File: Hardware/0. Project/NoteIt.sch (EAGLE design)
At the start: 61 parts, among them CN1 MICROSD-PUSH-OUT, CN3 USB 3.2 Gen 2 Type C Receptac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, CN4 FTSH-105-01-L-DV-K-TR, IC2 MCP73831/OT, IC5 S-8261ACMMD-G4MT2U, Q2 SI2374DSTRPBF, Q3 SI2374DSTRPBF, Q4 BC817-16LT1SMD, SW1 KY-040, U1 SN74AHC1G125, U10 MSP430FR2476TPTR, U2 GL823K, U4 TS3A27518EPWR, U5 TLV75530PDBVR, U8 DS3231/SO, X2 CRYSTAL-MINI

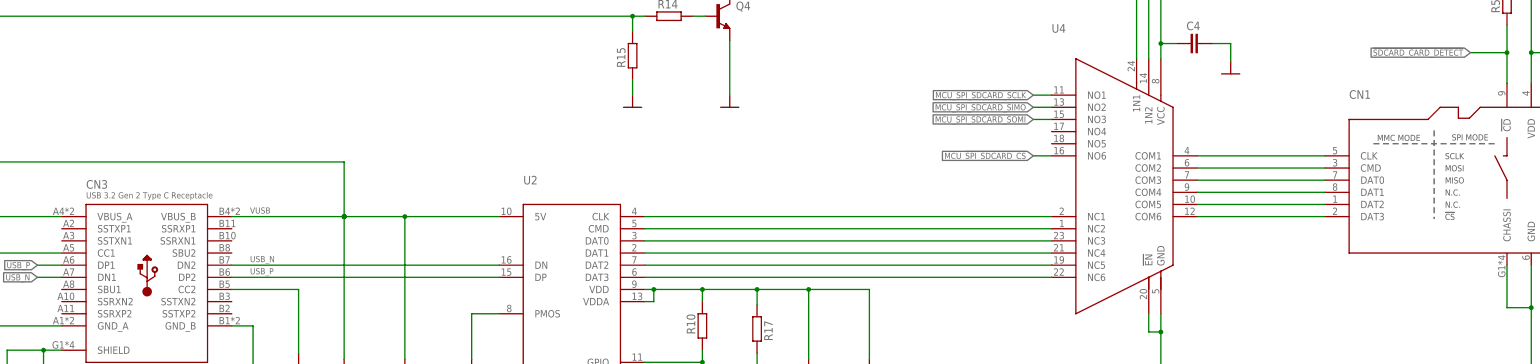
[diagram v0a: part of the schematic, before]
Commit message: SCH vs BRD conflicts fix
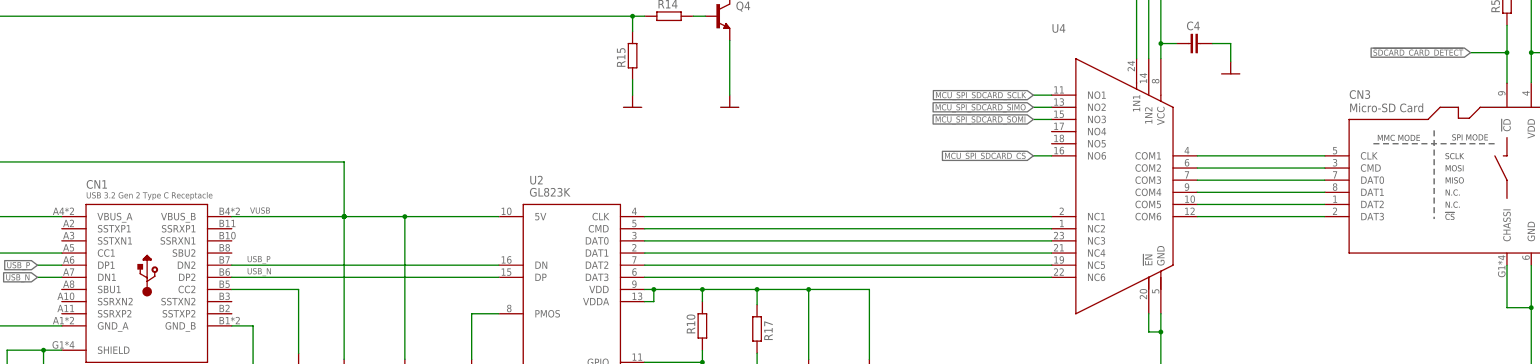
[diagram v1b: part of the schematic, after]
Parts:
- CN1: value MICROSD-PUSH-OUT -> USB 3.2 Gen 2 Type C Receptacle; device Micro SD:MICROSD-PUSH-OUT -> USB C CONNECOTR:USB4080-03-A
- CN3: value USB 3.2 Gen 2 Type C Receptacle -> Micro-SD Card; device USB C CONNECOTR:USB4080-03-A -> Micro SD:MICROSD-PUSH-OUT
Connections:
- net !SDCARD_CARD_DETECT!: now also CN3.!CD; no longer CN1.!CD
- net 0V: now also CN1.GND_A, CN1.GND_B, CN3.CHASSI, CN3.GND; no longer CN1.CHASSI, CN1.GND, CN3.GND_A, CN3.GND_B
- net 3.3V: now also CN3.VDD; no longer CN1.VDD
- net N$10: now also CN1.SHIELD; no longer CN3.SHIELD
- net N$15: now also CN3.CMD; no longer CN1.CMD
- net N$16: now also CN3.DAT0; no longer CN1.DAT0
- net N$2: now also CN3.CLK; no longer CN1.CLK
- net N$20: now also CN3.DAT1; no longer CN1.DAT1
- net N$21: now also CN1.CC2; no longer CN3.CC2
- net N$6: now also CN1.CC1; no longer CN3.CC1
- net N$7: now also CN3.DAT2; no longer CN1.DAT2
- net N$8: now also CN3.DAT3; no longer CN1.DAT3
- net USB_N: now also CN1.DN1, CN1.DP2, U2.DP; no longer CN3.DN1, CN3.DN2, U2.DN
- net USB_P: now also CN1.DN2, CN1.DP1, U2.DN; no longer CN3.DP1, CN3.DP2, U2.DP
- net VUSB: now also CN1.VBUS_A, CN1.VBUS_B; no longer CN3.VBUS_A, CN3.VBUS_B

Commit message: PCB design WIP
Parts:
- removed G1: CH291-1220LF, battery:CH291-1220LF
- added BAT1: CR1220, SamacSys_Parts:CR1220
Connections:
- net 0V: now also BAT1.-; no longer G1.-
- net N$22: now also BAT1.+; no longer G1.+
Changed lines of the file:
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@@
 <attribute name="PN" value="GRM188R61A106ME69D"/>
 </part>
-<part name="DS1" library="diy-modules" deviceset="DISPLAY-OLED-128X64" device="" value=""/>
+<part name="DS1" library="diy-modules" deviceset="DISPLAY-OLED-128X64" device="" package3d_urn="urn:adsk.eagle:package:32761919/2" value="DISPLAY-OLED-128X64"/>
 <part name="SUPPLY24" library="My-Supply" deviceset="3.3V" device=""/>
 <part name="C25" library="My-RLC" deviceset="C_" device="0603" package3d_urn="urn:adsk.eagle:package:23494015/2"/>
@@
 <part name="SUPPLY28" library="My-Supply" deviceset="0V" device=""/>
 <part name="SUPPLY29" library="My-Supply" deviceset="3.3V" device=""/>
-<part name="CN2" library="con-ptr500" deviceset="AK500/2-H" device="" package3d_urn="urn:adsk.eagle:package:9901/1"/>
+<part name="CN2" library="con-ptr500" deviceset="AK500/2-H" device="" package3d_urn="urn:adsk.eagle:package:9901/1" override_package3d_urn="urn:adsk.eagle:package:32815263/2" override_package_urn="urn:adsk.eagle:footprint:9865/1"/>
 <part name="SUPPLY32" library="My-Supply" deviceset="0V" device=""/>
 <part name="R1" library="My-RLC" deviceset="R_" device="0603" package3d_urn="urn:adsk.eagle:package:23494030/2"/>
@@
 <part name="SUPPLY42" library="My-Supply" deviceset="3.3V" device=""/>
 <part name="SUPPLY43" library="My-Supply" deviceset="3.3V" device=""/>
-<part name="G1" library="battery" library_urn="urn:adsk.eagle:library:109" deviceset="CH291-1220LF" device="" package3d_urn="urn:adsk.eagle:package:4617/1" value=""/>
 <part name="C14" library="My-RLC" deviceset="C_" device="0603" package3d_urn="urn:adsk.eagle:package:23494015/2"/>
 <part name="U8" library="adafruit" deviceset="DS3231" device="/SO" package3d_urn="urn:adsk.eagle:package:6240754/1" value=""/>
@@
 <part name="SUPPLY12" library="My-Supply" deviceset="0V" device=""/>
 <part name="CN3" library="Micro SD" deviceset="MICROSD-PUSH-OUT" device="" package3d_urn="urn:adsk.eagle:package:32766245/3" value="Micro-SD Card"/>
+<part name="BAT1" library="SamacSys_Parts" deviceset="CR1220" device=""/>
 </parts>
 <sheets>
@@
 <text x="226.06" y="363.22" size="1.778" layer="208" align="center" grouprefs="POWER_SUPPLY BATTERY_PROTECTOR">3.7V ~ 4.2V
 230mAh</text>
-<wire x1="247.65" y1="379.73" x2="247.65" y2="373.38" width="0.1524" layer="208" grouprefs="BATTERY_MONITOR POWER_SUPPLY"/>
-<wire x1="247.65" y1="373.38" x2="247.015" y2="374.65" width="0.1524" layer="208" grouprefs="BATTERY_MONITOR POWER_SUPPLY"/>
-<wire x1="247.015" y1="374.65" x2="248.285" y2="374.65" width="0.1524" layer="208" grouprefs="BATTERY_MONITOR POWER_SUPPLY"/>
-<wire x1="248.285" y1="374.65" x2="247.65" y2="373.38" width="0.1524" layer="208" grouprefs="BATTERY_MONITOR POWER_SUPPLY"/>
-<text x="253.111" y="376.682" size="1.27" layer="208" rot="R180" align="center" grouprefs="BATTERY_MONITOR POWER_SUPPLY">2.1μA max.</text>
-<text x="262.89" y="395.605" size="0.254" layer="201" align="center" grouprefs="BATTERY_MONITOR POWER_SUPPLY"> </text>
+<wire x1="247.65" y1="379.73" x2="247.65" y2="373.38" width="0.1524" layer="208" grouprefs="POWER_SUPPLY BATTERY_MONITOR"/>
+<wire x1="247.65" y1="373.38" x2="247.015" y2="374.65" width="0.1524" layer="208" grouprefs="POWER_SUPPLY BATTERY_MONITOR"/>
+<wire x1="247.015" y1="374.65" x2="248.285" y2="374.65" width="0.1524" layer="208" grouprefs="POWER_SUPPLY BATTERY_MONITOR"/>
+<wire x1="248.285" y1="374.65" x2="247.65" y2="373.38" width="0.1524" layer="208" grouprefs="POWER_SUPPLY BATTERY_MONITOR"/>
+<text x="253.111" y="376.682" size="1.27" layer="208" rot="R180" align="center" grouprefs="POWER_SUPPLY BATTERY_MONITOR">2.1μA max.</text>
+<text x="262.89" y="395.605" size="0.254" layer="201" align="center" grouprefs="POWER_SUPPLY BATTERY_MONITOR"> </text>
 <text x="182.88" y="395.605" size="0.254" layer="91" align="center" grouprefs="POWER_SUPPLY BATTERY_PROTECTOR"> </text>
 <text x="44.45" y="395.605" size="0.254" layer="91" align="center" grouprefs="BATTERY_CHARGING_MANAGER POWER_SUPPLY"> </text>
@@
 </instance>
 <instance part="SUPPLY14" gate="G$1" x="380.365" y="306.07" smashed="yes" grouprefs="POWER_SUPPLY"/>
-<instance part="R41" gate="G$1" x="245.745" y="358.14" smashed="yes" rot="R90" grouprefs="BATTERY_MONITOR POWER_SUPPLY">
+<instance part="R41" gate="G$1" x="245.745" y="358.14" smashed="yes" rot="R90" grouprefs="POWER_SUPPLY BATTERY_MONITOR">
 <attribute name="NAME" x="244.2464" y="355.6" size="1.778" layer="95" rot="R90"/>
 <attribute name="VALUE" x="249.047" y="355.6" size="1.778" layer="96" rot="R90"/>
 </instance>
-<instance part="R42" gate="G$1" x="245.745" y="342.9" smashed="yes" rot="R90" grouprefs="BATTERY_MONITOR POWER_SUPPLY">
+<instance part="R42" gate="G$1" x="245.745" y="342.9" smashed="yes" rot="R90" grouprefs="POWER_SUPPLY BATTERY_MONITOR">
 <attribute name="NAME" x="244.2464" y="340.36" size="1.778" layer="95" rot="R90"/>
 <attribute name="VALUE" x="249.047" y="340.36" size="1.778" layer="96" rot="R90"/>
@@
 <instance part="SUPPLY43" gate="G$1" x="301.625" y="125.73" smashed="yes" grouprefs="SPY-BY-WIRE_(ICSP)">
 <attribute name="VALUE" x="301.6504" y="129.54" size="1.778" layer="96" align="center"/>
-</instance>
-<instance part="G1" gate="G1" x="351.155" y="51.435" smashed="yes" rot="R90" grouprefs="REAL_TIME_CLOCK">
-<attribute name="NAME" x="347.345" y="50.165" size="1.778" layer="95" rot="R90"/>
-<attribute name="VALUE" x="356.235" y="46.99" size="1.778" layer="96" rot="R90"/>
 </instance>
 <instance part="C14" gate="G$1" x="339.725" y="52.07" smashed="yes" rot="R180" grouprefs="REAL_TIME_CLOCK">
@@
 <attribute name="NAME" x="342.265" y="231.648" size="1.778" layer="95"/>
 <attribute name="VALUE" x="342.265" y="228.854" size="1.778" layer="96"/>
+</instance>
+<instance part="BAT1" gate="G$1" x="351.155" y="51.435" smashed="yes">
+<attribute name="NAME" x="346.964" y="51.943" size="1.778" layer="95" rot="R90" align="center"/>
+<attribute name="VALUE" x="354.965" y="52.197" size="1.778" layer="96" rot="R90" align="center"/>
 </instance>
 </instances>
@@
 <pinref part="SUPPLY14" gate="G$1" pin="0V"/>
 <pinref part="R42" gate="G$1" pin="1"/>
-<wire x1="245.745" y1="337.82" x2="245.745" y2="313.69" width="0.1524" layer="91" grouprefs="BATTERY_MONITOR POWER_SUPPLY"/>
-<junction x="245.745" y="313.69" grouprefs="BATTERY_MONITOR POWER_SUPPLY"/>
+<wire x1="245.745" y1="337.82" x2="245.745" y2="313.69" width="0.1524" layer="91" grouprefs="POWER_SUPPLY BATTERY_MONITOR"/>
+<junction x="245.745" y="313.69" grouprefs="POWER_SUPPLY BATTERY_MONITOR"/>
 <pinref part="Q2" gate="G$1" pin="S"/>
 <pinref part="SUPPLY1" gate="G$1" pin="0V"/>
@@
 <wire x1="362.585" y1="45.085" x2="351.155" y2="45.085" width="0.1524" layer="91" grouprefs="REAL_TIME_CLOCK"/>
 <junction x="339.725" y="45.085" grouprefs="REAL_TIME_CLOCK"/>
-<pinref part="G1" gate="G1" pin="-"/>
 <wire x1="351.155" y1="45.085" x2="339.725" y2="45.085" width="0.1524" layer="91" grouprefs="REAL_TIME_CLOCK"/>
 <wire x1="351.155" y1="46.355" x2="351.155" y2="45.085" width="0.1524" layer="91" grouprefs="REAL_TIME_CLOCK"/>
@@
 <pinref part="U8" gate="G$1" pin="GND"/>
 <pinref part="SUPPLY15" gate="G$1" pin="0V"/>
+<pinref part="BAT1" gate="G$1" pin="-"/>
 </segment>
 <segment>
@@
 <junction x="311.785" y="376.555" grouprefs="VOLTAGE_REGULATOR POWER_SUPPLY"/>
 <pinref part="R41" gate="G$1" pin="2"/>
-<wire x1="245.745" y1="363.22" x2="245.745" y2="381.635" width="0.1524" layer="91" grouprefs="BATTERY_MONITOR POWER_SUPPLY"/>
-<junction x="245.745" y="381.635" grouprefs="BATTERY_MONITOR POWER_SUPPLY"/>
+<wire x1="245.745" y1="363.22" x2="245.745" y2="381.635" width="0.1524" layer="91" grouprefs="POWER_SUPPLY BATTERY_MONITOR"/>
+<junction x="245.745" y="381.635" grouprefs="POWER_SUPPLY BATTERY_MONITOR"/>
 </segment>
 </net>
@@
 <pinref part="R41" gate="G$1" pin="1"/>
 <pinref part="R42" gate="G$1" pin="2"/>
-<wire x1="245.745" y1="347.98" x2="245.745" y2="350.52" width="0.1524" layer="91" grouprefs="BATTERY_MONITOR POWER_SUPPLY"/>
-<wire x1="245.745" y1="350.52" x2="245.745" y2="353.06" width="0.1524" layer="91" grouprefs="BATTERY_MONITOR POWER_SUPPLY"/>
-<wire x1="245.745" y1="350.52" x2="253.365" y2="350.52" width="0.1524" layer="91" grouprefs="BATTERY_MONITOR POWER_SUPPLY"/>
-<junction x="245.745" y="350.52" grouprefs="BATTERY_MONITOR POWER_SUPPLY"/>
-<label x="253.365" y="350.52" size="1.27" layer="95" xref="yes" grouprefs="BATTERY_MONITOR POWER_SUPPLY"/>
+<wire x1="245.745" y1="347.98" x2="245.745" y2="350.52" width="0.1524" layer="91" grouprefs="POWER_SUPPLY BATTERY_MONITOR"/>
+<wire x1="245.745" y1="350.52" x2="245.745" y2="353.06" width="0.1524" layer="91" grouprefs="POWER_SUPPLY BATTERY_MONITOR"/>
+<wire x1="245.745" y1="350.52" x2="253.365" y2="350.52" width="0.1524" layer="91" grouprefs="POWER_SUPPLY BATTERY_MONITOR"/>
+<junction x="245.745" y="350.52" grouprefs="POWER_SUPPLY BATTERY_MONITOR"/>
+<label x="253.365" y="350.52" size="1.27" layer="95" xref="yes" grouprefs="POWER_SUPPLY BATTERY_MONITOR"/>
 </segment>
 </net>
@@
 <net name="N$22" class="0">
 <segment>
-<pinref part="G1" gate="G1" pin="+"/>
 <wire x1="362.585" y1="57.785" x2="351.155" y2="57.785" width="0.1524" layer="91" grouprefs="REAL_TIME_CLOCK"/>
 <wire x1="351.155" y1="57.785" x2="351.155" y2="56.515" width="0.1524" layer="91" grouprefs="REAL_TIME_CLOCK"/>
 <pinref part="U8" gate="G$1" pin="VBAT"/>
-</segment>
-</net>
+<pinref part="BAT1" gate="G$1" pin="+"/>
+</segment>
+</net>

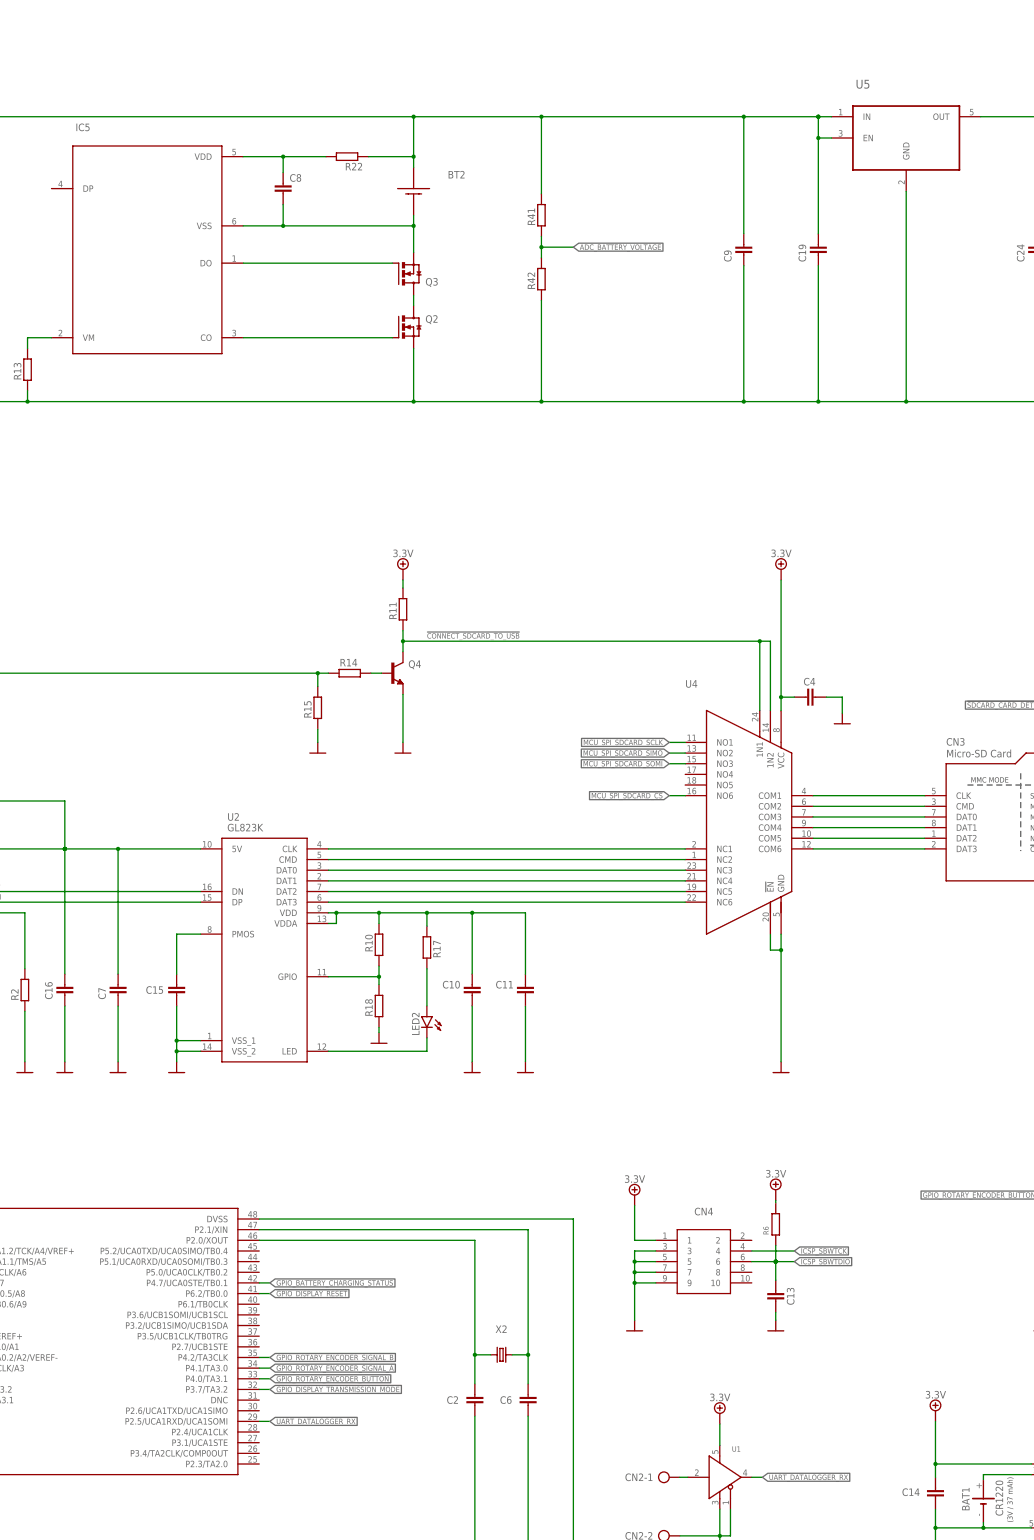
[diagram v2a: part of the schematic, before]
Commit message: Standardization footprints from the same package type
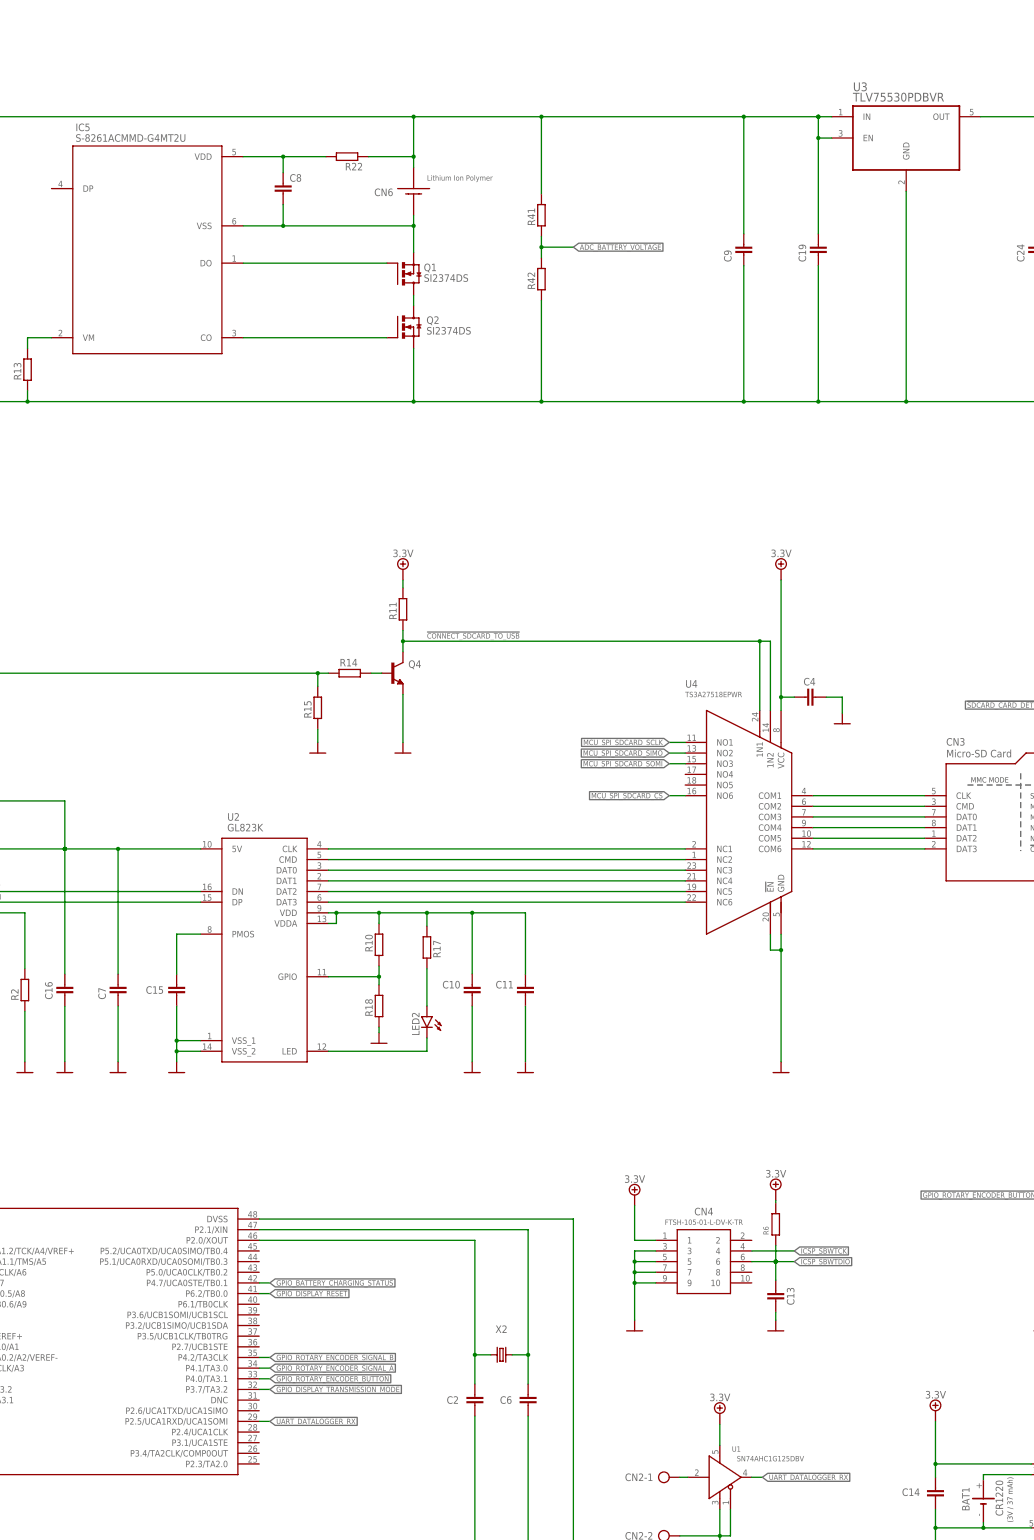
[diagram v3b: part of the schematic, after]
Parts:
- removed BT2: LiPO, Battery:BATERIA
- removed Q3: SI2374DSTRPBF, SI2374DS:SI2374DSTRPBF
- added CN6: Lithium Ion Polymer, Battery:BATTERYJST-2
- added Q1: SI2374DS, SI2374DS:SI2374DSSOT23
- Q2: value SI2374DSTRPBF -> SI2374DS; device SI2374DS:SI2374DSTRPBF -> SI2374DS:SI2374DSSOT23
- U1: value SN74AHC1G125 -> SN74AHC1G125DBV; device SN74AHC1G125DRLR:SN74AHC1G125 -> SN74AHC1G125DRLR:SN74AHC1G125DBV
- renumbered U5 to U3
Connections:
- net N$1: now also Q1.G; no longer Q3.G
- net N$3: now also Q1.D; no longer Q3.D
- net N$32: now also CN6.GND, Q1.S; no longer BT2.GND, Q3.S
- net N$33: now also CN6.VDD; no longer BT2.VDD
- net N$4: now also U1.IN; no longer U1.A
- net UART_DATALOGGER_RX: now also U1.OUT; no longer U1.Y
